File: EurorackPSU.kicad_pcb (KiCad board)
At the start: 4 copper layers, 127 x 152.4 mm, 42 parts, among them J2 Conn_01x03_Male, J4 Conn_01x03_Male, U1 lt8638s, U2 lt8638s

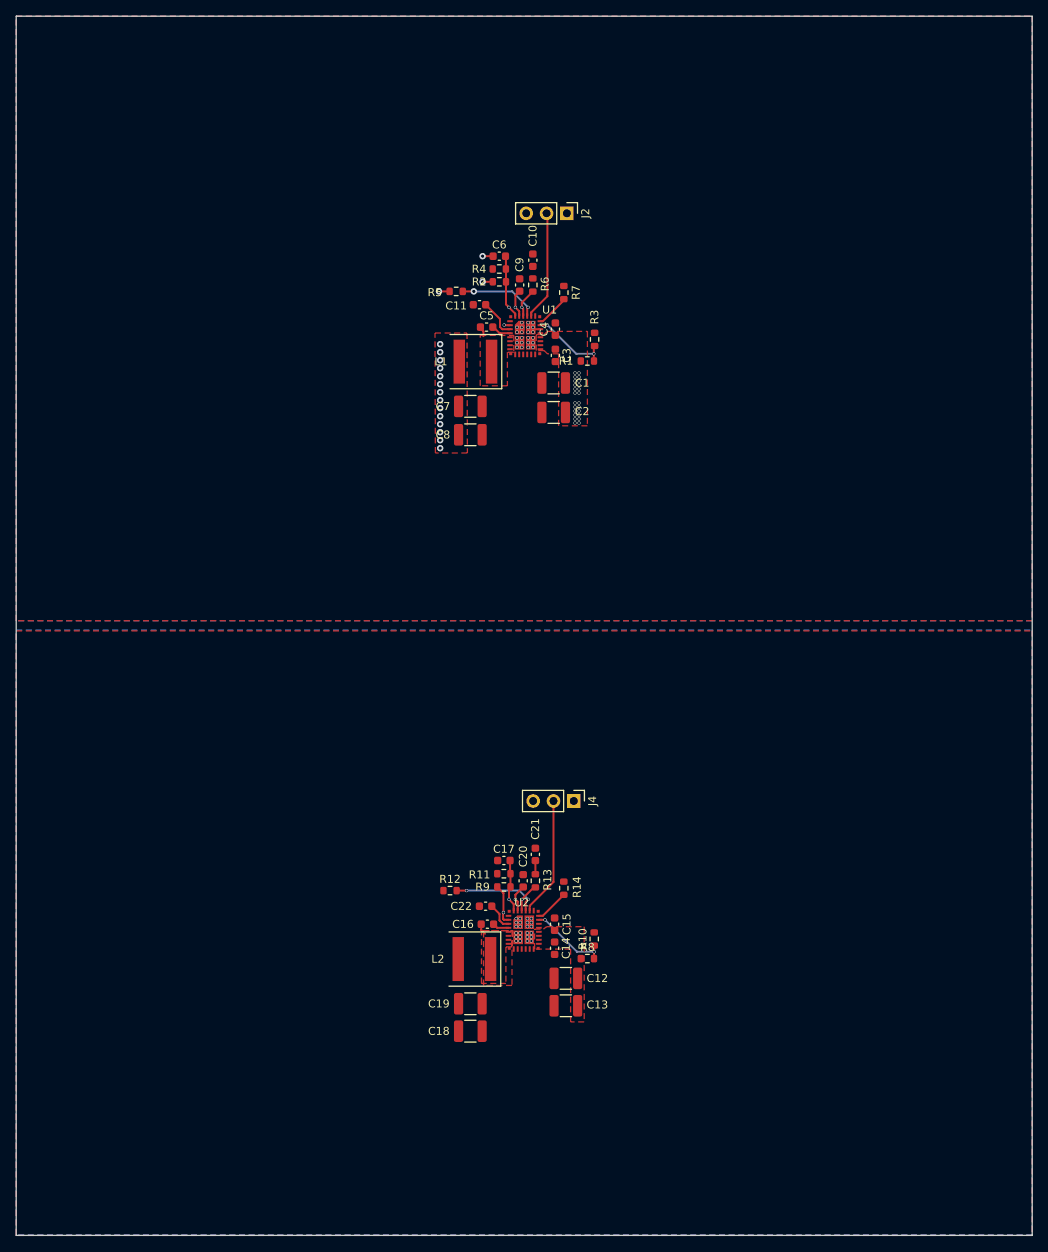
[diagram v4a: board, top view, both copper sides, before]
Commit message: Initial connector placement and more power plane setup
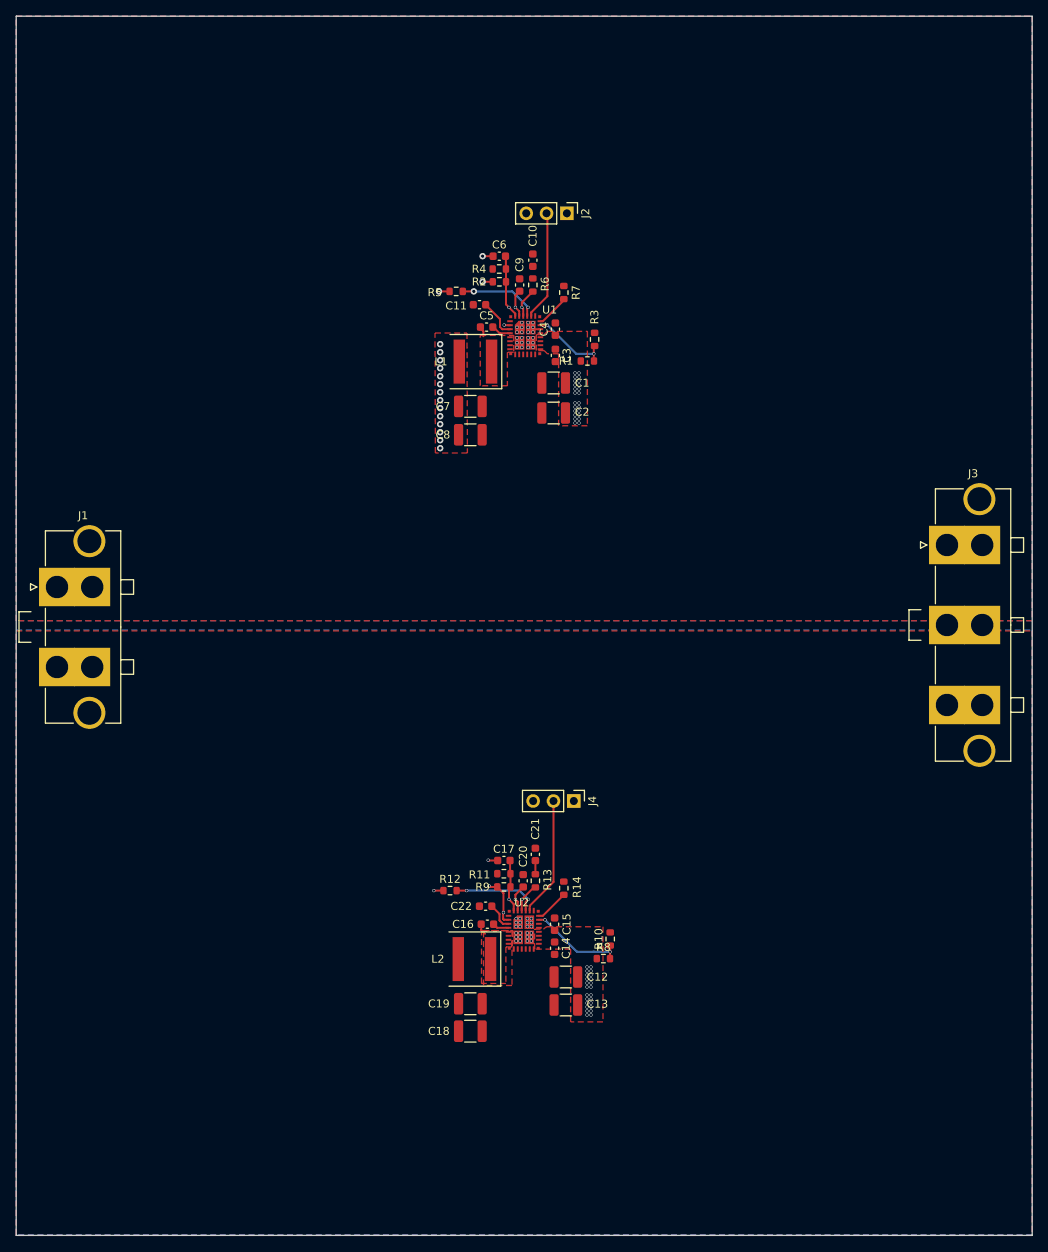
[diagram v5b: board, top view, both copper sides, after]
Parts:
- added J1: Conn_01x02, Connector_Molex:Molex_Mini-Fit_Sr_42819-22XX_1x02_P10.00mm_Vertical, F.Cu at (30.5, 96.8)
- added J3: Conn_01x03, Connector_Molex:Molex_Mini-Fit_Sr_42819-32XX_1x03_P10.00mm_Vertical, F.Cu at (141.8, 91.5)
- moved R10 2.00 mm to (99.7, 140.8)
- moved R8 2.00 mm to (98.8, 143.2)
- moved C12 0.17 mm to (94.1, 145.5)
- moved C13 0.10 mm to (94.1, 149.0)
- moved C2 0.07 mm to (92.6, 75.0)
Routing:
- net GND: track 6.34 -> 9.84 mm, vias 24 -> 27
- net Net-(R10-Pad1): track 10.2 -> 12.4 mm
- net Net-(C1-Pad1): vias 24 -> 48
- added copper zone on In1.Cu, net GND

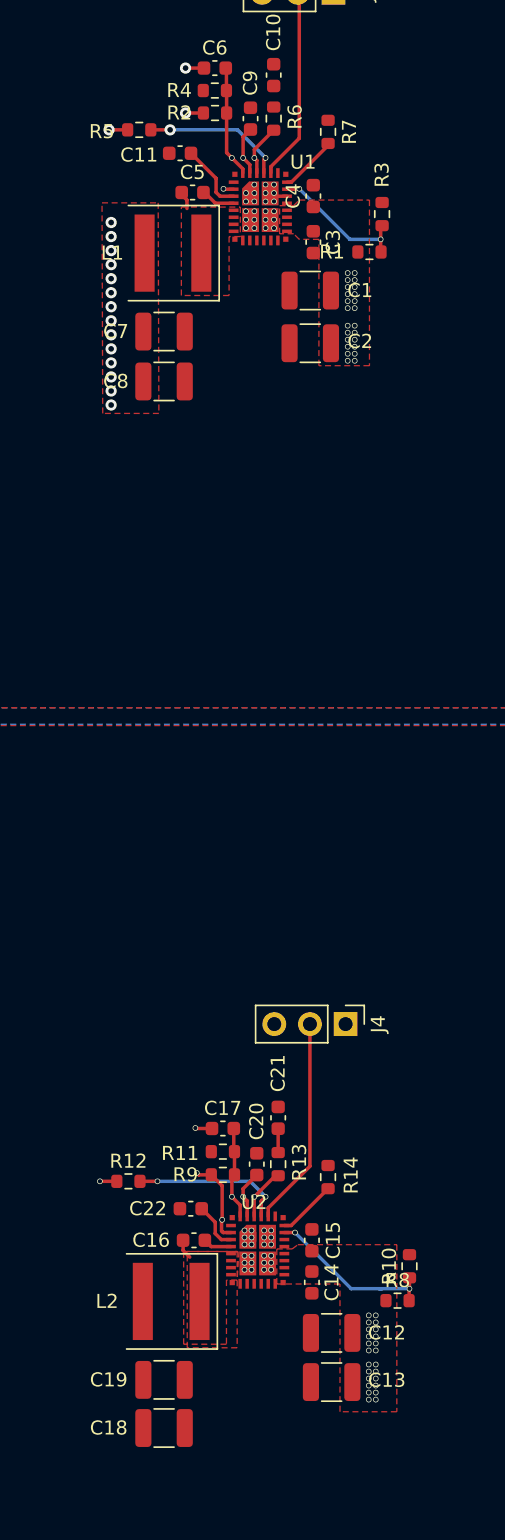
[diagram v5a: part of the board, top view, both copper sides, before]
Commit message: Added net name for power input, added more vias, and more
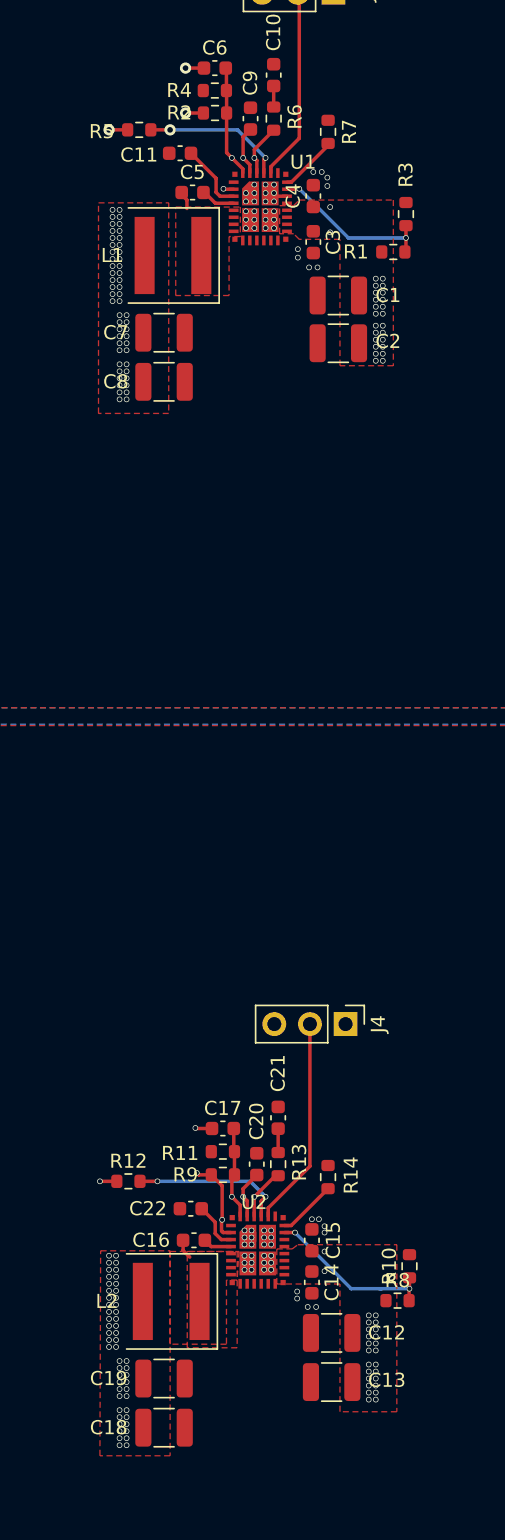
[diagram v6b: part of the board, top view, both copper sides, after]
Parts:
- moved C1 2.03 mm to (94.6, 71.6)
- moved C2 2.00 mm to (94.6, 75.0)
- moved R1 1.70 mm to (98.5, 68.5)
- moved R3 1.70 mm to (99.4, 65.8)
- moved L1 0.17 mm to (82.8, 68.8)
- moved C19 0.09 mm to (82.2, 148.8)
- moved C7 0.08 mm to (82.2, 74.2)
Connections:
- net Net-(C1-Pad1) renamed +VDC
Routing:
- net Net-(R1-Pad2): track 10.3 -> 12.0 mm
- net Net-(C10-Pad1): track 0.00 -> 1.50 mm
- net GND: vias 27 -> 87
- net -12V: vias 24 -> 32
- net +VDC: vias 48 -> 52
- net +12V: vias 18 -> 56
